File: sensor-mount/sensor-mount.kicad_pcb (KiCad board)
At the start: 2 copper layers, 10 x 10 mm, 4 parts, among them U1 MAX31725

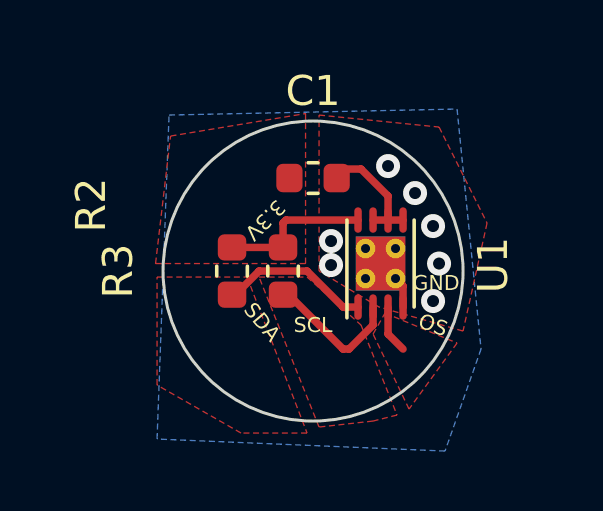
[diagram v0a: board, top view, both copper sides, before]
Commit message: The Maxim footprint has 0.65mm pitch.
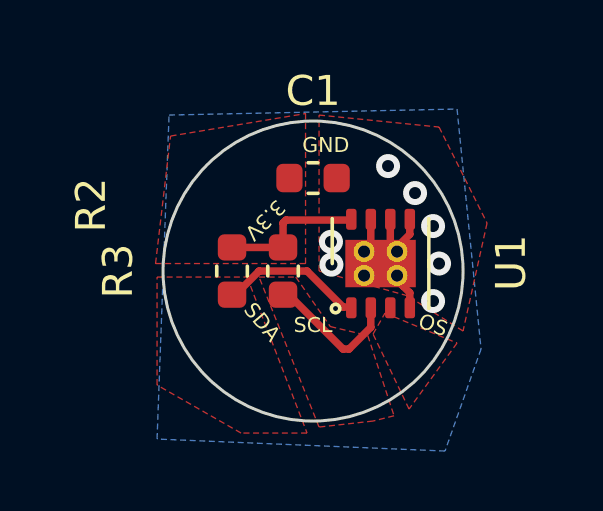
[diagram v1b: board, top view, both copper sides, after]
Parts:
- U1: footprint Package_DFN_QFN:TDFN-8-1EP_3x2mm_P0.5mm_EP1.80x1.65mm_ThermalVias -> maxim-8tdfn-vias:DFN-8-1EP_3x3mm_P0.65mm_EP1.7x2.05mm
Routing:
- net GND: track 4.94 -> 7.23 mm
- net /OS: track 1.61 -> 0.00 mm
